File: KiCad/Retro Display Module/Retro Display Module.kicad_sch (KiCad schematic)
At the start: 37 parts, among them J1 VCC, J10 CFG, J11 SEL, J12 GND, J13 Conn_02x03_Odd_Even, J2 TX, J3 RX, J4 CFG, J5 SEL, J6 GND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

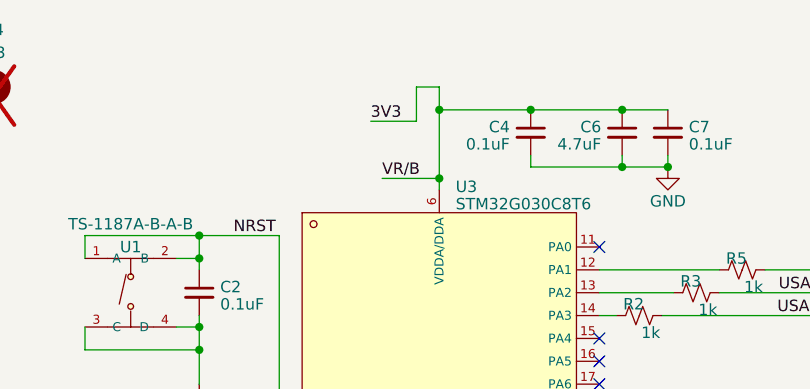
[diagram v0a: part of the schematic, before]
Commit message: Added reverse polarity protection
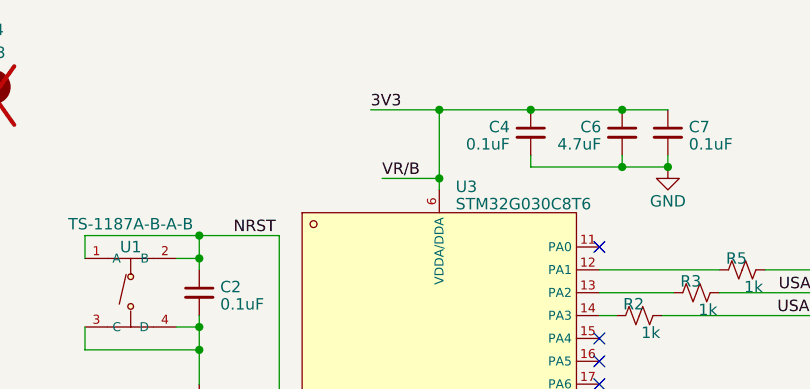
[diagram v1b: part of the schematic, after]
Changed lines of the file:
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@@
-    (stroke (width 0) (type default))
-  )
-  (wire (pts (xy 88.9 27.94) (xy 88.9 24.13))
     (stroke (width 0) (type default))
   )
@@
     (stroke (width 0) (type default))
   )
-  (wire (pts (xy 88.9 24.13) (xy 91.44 24.13))
+  (wire (pts (xy 83.82 26.67) (xy 91.44 26.67))
     (stroke (width 0) (type default))
   )
@@
   )
   (wire (pts (xy 64.77 50.8) (xy 64.77 53.34))
-    (stroke (width 0) (type default))
-  )
-  (wire (pts (xy 83.82 27.94) (xy 88.9 27.94))
     (stroke (width 0) (type default))
   )
@@
     (stroke (width 0) (type default))
   )
-  (wire (pts (xy 91.44 24.13) (xy 91.44 26.67))
-    (stroke (width 0) (type default))
-  )
   (wire (pts (xy 160.02 66.04) (xy 175.26 66.04))
     (stroke (width 0) (type default))
@@
     (effects (font (size 1.27 1.27)) (justify right bottom))
   )
-  (label "3V3" (at 83.82 27.94 0) (fields_autoplaced)
+  (label "3V3" (at 83.82 26.67 0) (fields_autoplaced)
     (effects (font (size 1.27 1.27)) (justify left bottom))
   )
